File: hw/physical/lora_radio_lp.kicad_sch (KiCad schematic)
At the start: 0 parts

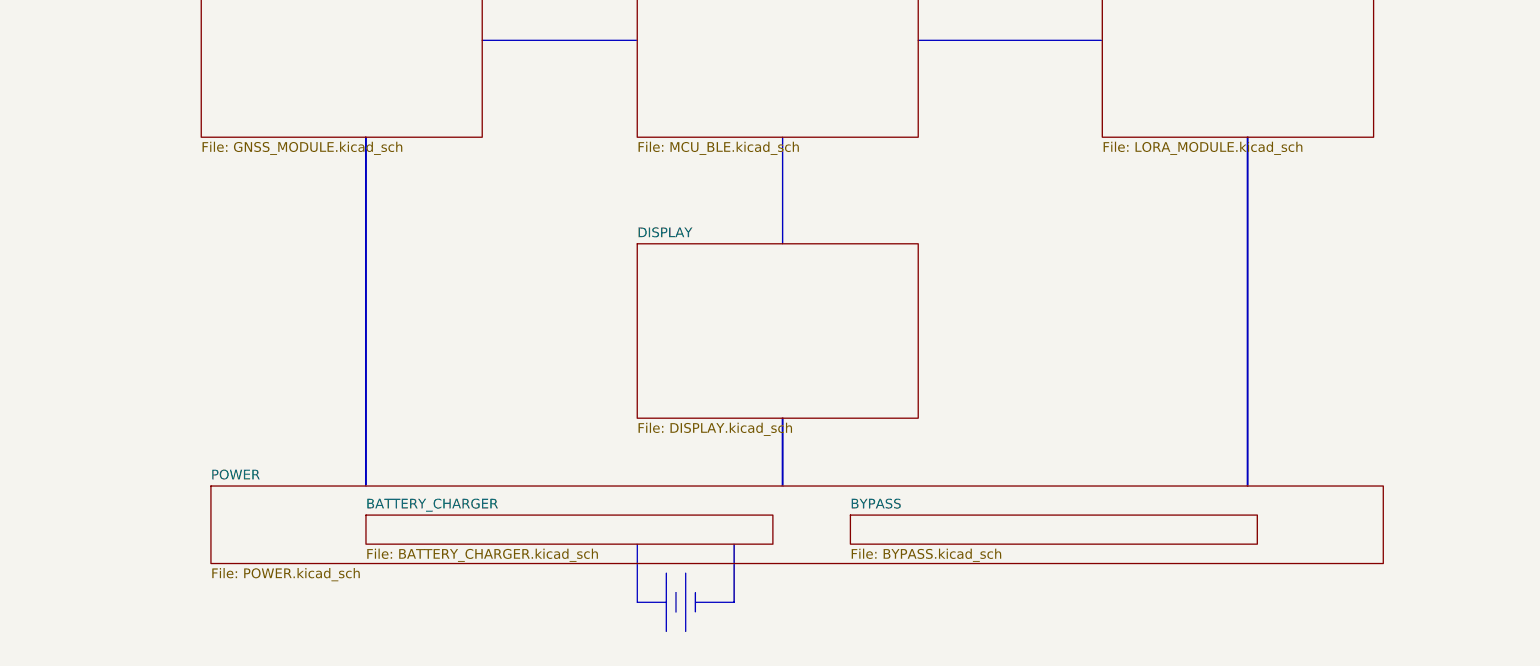
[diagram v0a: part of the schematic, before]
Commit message: - Consolidate POWER and BATTERY pages - Updated 1.8V SYS REG to low Iq option - Replaced LoRA module with SemTech transceiver - Adding latest nRF datasheet
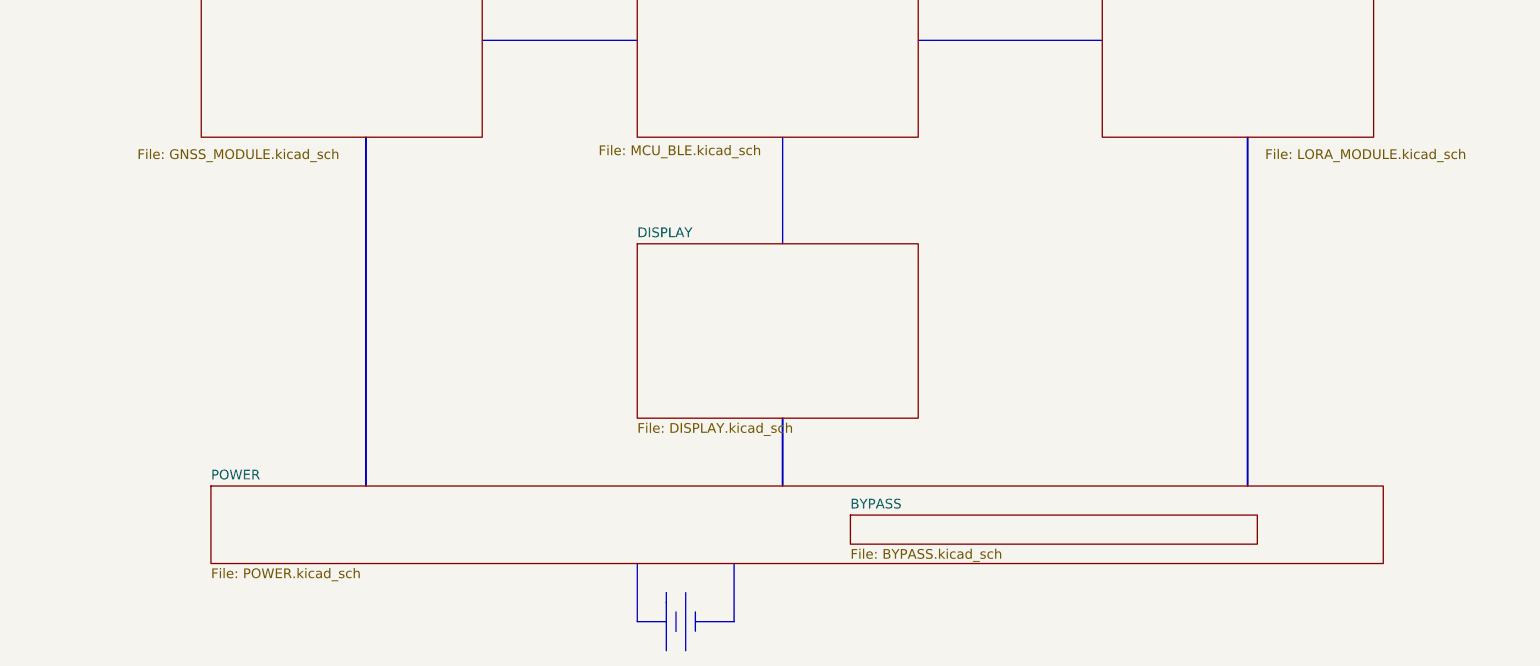
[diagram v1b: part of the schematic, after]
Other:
- removed sheet BATTERY_CHARGER
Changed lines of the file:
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@@
 	(polyline
 		(pts
-			(xy 158.75 177.8) (xy 158.75 170.18)
+			(xy 158.75 180.34) (xy 158.75 172.72)
 		)
 		(stroke
@@
 	(polyline
 		(pts
-			(xy 152.4 166.37) (xy 152.4 173.99)
+			(xy 152.4 168.91) (xy 152.4 176.53)
 		)
 		(stroke
@@
 	(polyline
 		(pts
-			(xy 160.02 175.26) (xy 160.02 172.72)
+			(xy 160.02 177.8) (xy 160.02 175.26)
 		)
 		(stroke
@@
 	(polyline
 		(pts
-			(xy 156.21 177.8) (xy 156.21 171.45)
+			(xy 156.21 180.34) (xy 156.21 173.99)
 		)
 		(stroke
@@
 	(polyline
 		(pts
-			(xy 156.21 171.45) (xy 156.21 170.18)
-		)
-		(stroke
-			(width 0)
-			(type default)
-		)
-	)
-	(polyline
-		(pts
-			(xy 157.48 175.26) (xy 157.48 172.72)
+			(xy 156.21 173.99) (xy 156.21 172.72)
+		)
+		(stroke
+			(width 0)
+			(type default)
+		)
+	)
+	(polyline
+		(pts
+			(xy 157.48 177.8) (xy 157.48 175.26)
 		)
 		(stroke
@@
 	(polyline
 		(pts
-			(xy 152.4 173.99) (xy 156.21 173.99)
+			(xy 152.4 176.53) (xy 156.21 176.53)
 		)
 		(stroke
@@
 	(polyline
 		(pts
-			(xy 160.02 173.99) (xy 165.1 173.99)
+			(xy 160.02 176.53) (xy 165.1 176.53)
 		)
 		(stroke
@@
 	(polyline
 		(pts
-			(xy 165.1 166.37) (xy 165.1 173.99)
+			(xy 165.1 168.91) (xy 165.1 176.53)
 		)
 		(stroke
@@
 		(at 152.4 90.17)
 		(size 36.83 22.86)
-		(fields_autoplaced yes)
 		(stroke
 			(width 0.1524)
@@
 		)
 		(property "Sheetfile" "MCU_BLE.kicad_sch"
-			(at 152.4 113.6146 0)
+			(at 147.32 114.046 0)
 			(effects
 				(font
@@
 		(at 95.25 90.17)
 		(size 36.83 22.86)
-		(fields_autoplaced yes)
 		(stroke
 			(width 0.1524)
@@
 		)
 		(property "Sheetfile" "GNSS_MODULE.kicad_sch"
-			(at 95.25 113.6146 0)
+			(at 86.868 114.554 0)
 			(effects
 				(font
@@
 		(at 213.36 90.17)
 		(size 35.56 22.86)
-		(fields_autoplaced yes)
 		(stroke
 			(width 0.1524)
@@
 		)
 		(property "Sheetfile" "LORA_MODULE.kicad_sch"
-			(at 213.36 113.6146 0)
+			(at 234.696 114.554 0)
 			(effects
 				(font
@@
 				)
 			)
-		)
-	)
-	(sheet
-		(at 116.84 162.56)
-		(size 53.34 3.81)
-		(fields_autoplaced yes)
-		(stroke
-			(width 0.1524)
-			(type solid)
-		)
-		(fill
-			(color 0 0 0 0.0000)
-		)
-		(property "Sheetname" "BATTERY_CHARGER"
-			(at 116.84 161.8484 0)
-			(effects
-				(font
-					(size 1.27 1.27)
-				)
-				(justify left bottom)
-			)
-		)
-		(property "Sheetfile" "BATTERY_CHARGER.kicad_sch"
-			(at 116.84 166.9546 0)
-			(effects
-				(font
-					(size 1.27 1.27)
-				)
-				(justify left top)
-			)
-		)
-		(instances
-			(project "lora_radio_lp"
-				(path "/fff85bc4-e8ec-4b5d-b2e2-83ecb397a864"
-					(page "8")
-				)
-			)

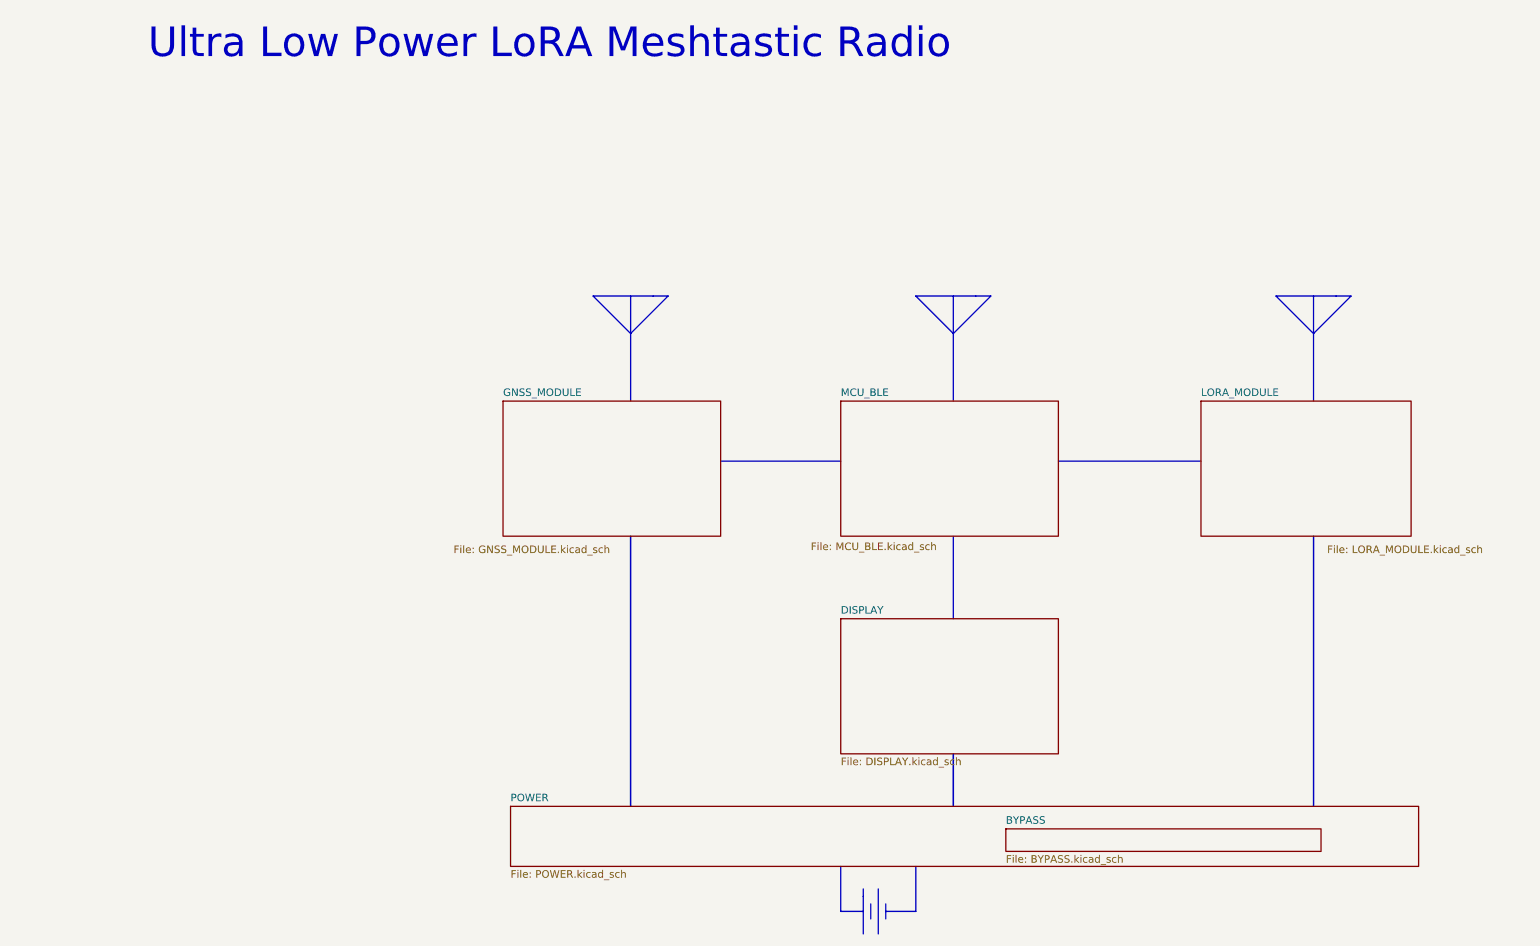
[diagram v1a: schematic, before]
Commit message: Various Schematic Modifications and Additions. * Removed Bypass page and moved bypass caps to MCU page. * Moved MCU VSS_PA pin to logical location as per Nordic guidelines. * Added Display Circuit, level shifters, charge pump, connector, etc. * Added 3.3V display VREG with Enable GPIO. * Added BLE RF components as per Nordic guidelines. * Added DCC circuit as per Nordic guidelines. * Rearranged GPIO's and interfaces. * Fixed various schematic errors.
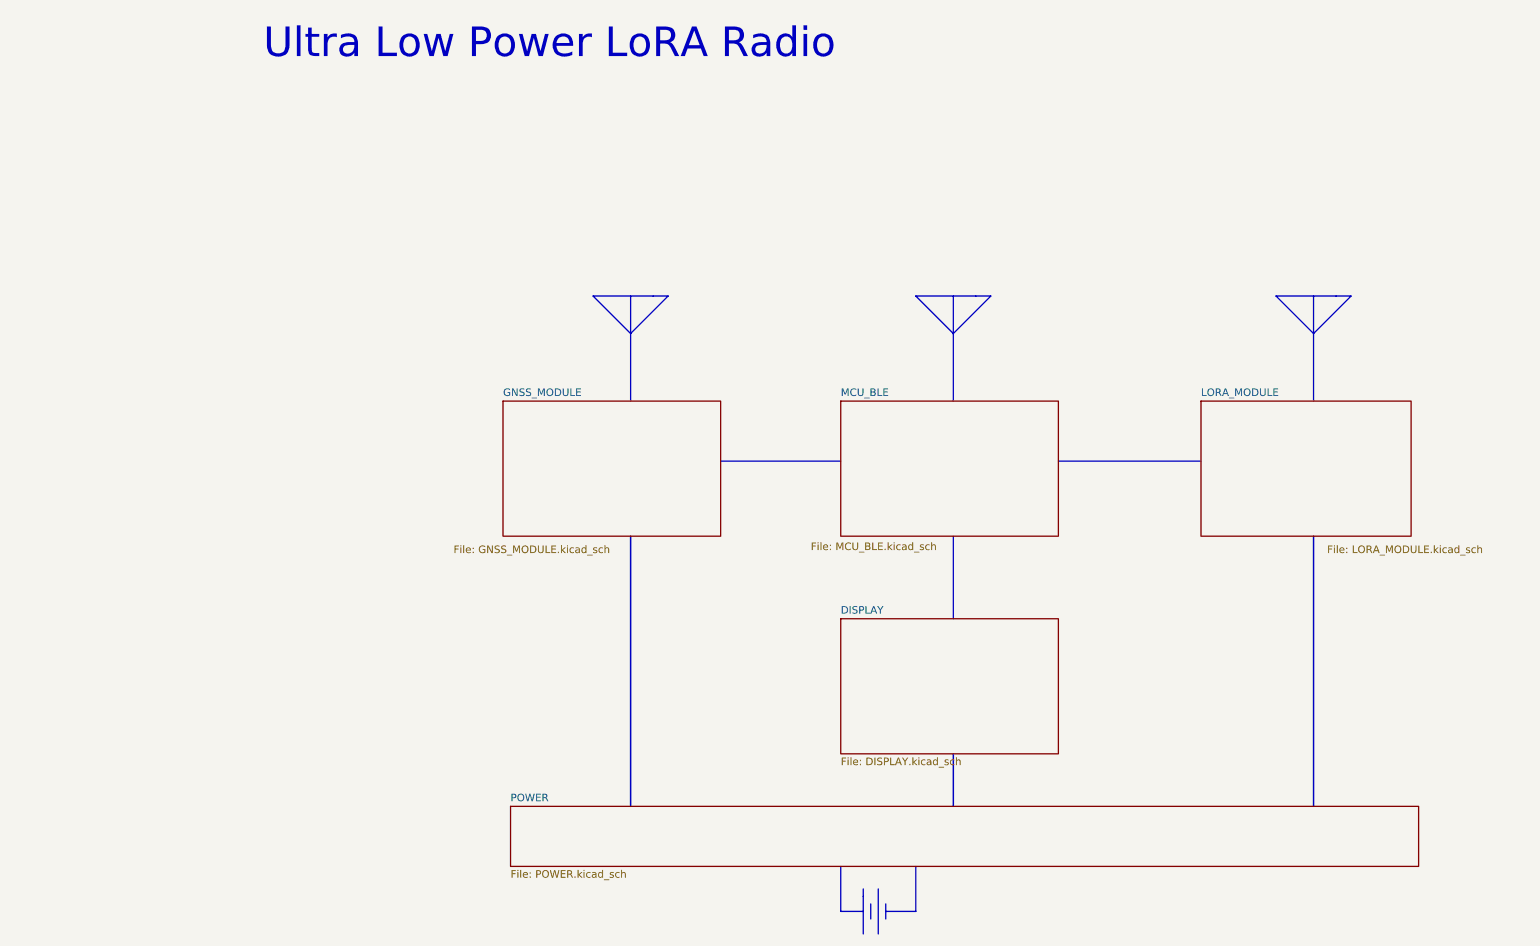
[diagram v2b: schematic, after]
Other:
- removed sheet BYPASS
- note added: "Ultra Low Power LoRA Radio"
- note removed: "Ultra Low Power LoRA Meshtastic Radio"
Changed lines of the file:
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@@
 		)
 	)
-	(text "Ultra Low Power LoRA Meshtastic Radio"
+	(text "Ultra Low Power LoRA Radio"
 		(exclude_from_sim no)
 		(at 103.124 29.718 0)
@@
 	)
 	(sheet
-		(at 180.34 162.56)
-		(size 53.34 3.81)
-		(fields_autoplaced yes)
-		(stroke
-			(width 0.1524)
-			(type solid)
-		)
-		(fill
-			(color 0 0 0 0.0000)
-		)
-		(property "Sheetname" "BYPASS"
-			(at 180.34 161.8484 0)
-			(effects
-				(font
-					(size 1.27 1.27)
-				)
-				(justify left bottom)
-			)
-		)
-		(property "Sheetfile" "BYPASS.kicad_sch"
-			(at 180.34 166.9546 0)
-			(effects
-				(font
-					(size 1.27 1.27)
-				)
-				(justify left top)
-			)
-		)
-		(instances
-			(project "lora_radio_lp"
-				(path "/fff85bc4-e8ec-4b5d-b2e2-83ecb397a864"
-					(page "6")
-				)
-			)
-		)
-	)
-	(sheet
 		(at 96.52 158.75)
 		(size 153.67 10.16)
@@
 			(project "lora_radio_lp"
 				(path "/fff85bc4-e8ec-4b5d-b2e2-83ecb397a864"
-					(page "7")
+					(page "6")
 				)
 			)
